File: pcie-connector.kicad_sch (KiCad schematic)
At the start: 7 parts, among them J2 PCIe_x16_10146070-113Y0LF-ver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

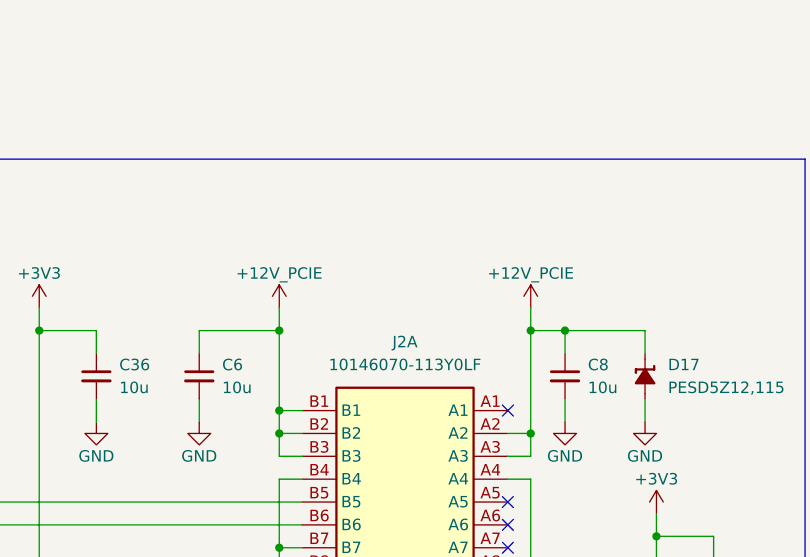
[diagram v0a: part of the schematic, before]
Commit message: [#79426] Removed power sequencing, added PERST control
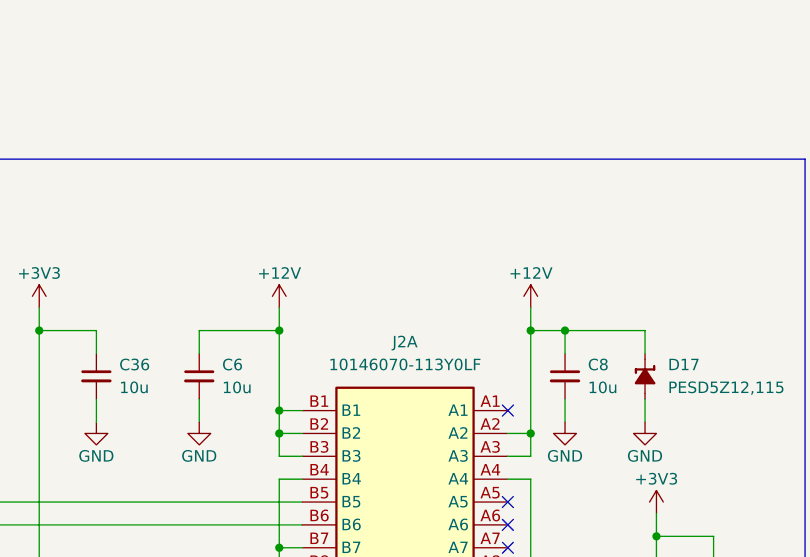
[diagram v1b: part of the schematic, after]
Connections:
- net +12V_PCIE renamed +12V
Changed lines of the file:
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@@
-	)
-	(symbol
-		(lib_id "antmicropower:+12V")
-		(at 147.32 91.44 0)
-		(unit 1)
-		(exclude_from_sim no)
-		(in_bom yes)
-		(on_board yes)
-		(dnp no)
-		(property "Reference" "#PWR06"
-			(at 147.32 95.25 0)
-			(effects
-				(font
-					(size 1.27 1.27)
-				)
-				(hide yes)
-			)
-		)
-		(property "Value" "+12V_PCIE"
-			(at 147.32 87.63 0)
-			(effects
-				(font
-					(size 1.27 1.27)
-				)
-			)
-		)
-		(property "Footprint" ""
-			(at 147.32 91.44 0)
-			(effects
-				(font
-					(size 1.27 1.27)
-				)
-				(hide yes)
-			)
-		)
-		(property "Datasheet" ""
-			(at 147.32 91.44 0)
-			(effects
-				(font
-					(size 1.27 1.27)
-				)
-				(hide yes)
-			)
-		)
-		(property "Description" ""
-			(at 147.32 91.44 0)
-			(effects
-				(font
-					(size 1.27 1.27)
-				)
-				(hide yes)
-			)
-		)
-		(pin "1"
-		)
-		(instances
-			(project "oculink-to-pcie-adapter"
-				(path "/44c3be85-0a18-4d93-a9a5-650ee09b6032/1dd577d8-5fbf-46d4-a369-3d141c3fbf7d"
-					(reference "#PWR06")
-					(unit 1)
-				)
-			)
-		)
 	)
 	(symbol
@@
 	)
 	(symbol
+		(lib_id "antmicropower:+12V_AON")
+		(at 147.32 91.44 0)
+		(unit 1)
+		(exclude_from_sim no)
+		(in_bom yes)
+		(on_board yes)
+		(dnp no)
+		(property "Reference" "#PWR06"
+			(at 147.32 95.25 0)
+			(effects
+				(font
+					(size 1.27 1.27)
+				)
+				(hide yes)
+			)
+		)
+		(property "Value" "+12V"
+			(at 147.32 87.63 0)
+			(effects
+				(font
+					(size 1.27 1.27)
+				)
+			)
+		)
+		(property "Footprint" ""
+			(at 147.32 91.44 0)
+			(effects
+				(font
+					(size 1.27 1.27)
+				)
+				(hide yes)
+			)
+		)
+		(property "Datasheet" ""
+			(at 147.32 91.44 0)
+			(effects
+				(font
+					(size 1.27 1.27)
+				)
+				(hide yes)
+			)
+		)
+		(property "Description" ""
+			(at 147.32 91.44 0)
+			(effects
+				(font
+					(size 1.27 1.27)
+				)
+				(hide yes)
+			)
+		)
+		(pin "1"
+		)
+		(instances
+			(project "oculink-to-pcie-adapter"
+				(path "/44c3be85-0a18-4d93-a9a5-650ee09b6032/1dd577d8-5fbf-46d4-a369-3d141c3fbf7d"
+					(reference "#PWR06")
+					(unit 1)
+				)
+			)
+		)
+	)
+	(symbol
 		(lib_id "antmicropower:GND")
 		(at 292.1 208.28 0)
@@
 	)
 	(symbol
+		(lib_id "antmicropower:+12V_AON")
+		(at 175.26 91.44 0)
+		(unit 1)
+		(exclude_from_sim no)
+		(in_bom yes)
+		(on_board yes)
+		(dnp no)
+		(property "Reference" "#PWR03"
+			(at 175.26 95.25 0)
+			(effects
+				(font
+					(size 1.27 1.27)
+				)
+				(hide yes)
+			)
+		)
+		(property "Value" "+12V"
+			(at 175.26 87.63 0)
+			(effects
+				(font
+					(size 1.27 1.27)
+				)
+			)
+		)
+		(property "Footprint" ""
+			(at 175.26 91.44 0)
+			(effects
+				(font
+					(size 1.27 1.27)
+				)
+				(hide yes)
+			)
+		)
+		(property "Datasheet" ""
+			(at 175.26 91.44 0)
+			(effects
+				(font
+					(size 1.27 1.27)
+				)
+				(hide yes)
+			)
+		)
+		(property "Description" ""
+			(at 175.26 91.44 0)
+			(effects
+				(font
+					(size 1.27 1.27)
+				)
+				(hide yes)
+			)
+		)
+		(pin "1"
+		)
+		(instances
+			(project "oculink-to-pcie-adapter"
+				(path "/44c3be85-0a18-4d93-a9a5-650ee09b6032/1dd577d8-5fbf-46d4-a369-3d141c3fbf7d"
+					(reference "#PWR03")
+					(unit 1)
+				)
+			)
+		)
+	)
+	(symbol
 		(lib_id "antmicroTVSDiodes:PESD5Z12")
 		(at 187.96 96.52 270)
@@
 					(unit 1)
 				)
-			)
-		)
-	)
-	(symbol
-		(lib_id "antmicropower:+12V")
-		(at 175.26 91.44 0)
-		(unit 1)
-		(exclude_from_sim no)
-		(in_bom yes)
-		(on_board yes)
-		(dnp no)
-		(property "Reference" "#PWR03"
-			(at 175.26 95.25 0)
-			(effects
-				(font
-					(size 1.27 1.27)
-				)
-				(hide yes)
-			)
-		)
-		(property "Value" "+12V_PCIE"
-			(at 175.26 87.63 0)
-			(effects
-				(font
-					(size 1.27 1.27)
-				)
-			)
-		)
-		(property "Footprint" ""
-			(at 175.26 91.44 0)
-			(effects
-				(font
-					(size 1.27 1.27)
-				)
-				(hide yes)
-			)
-		)
-		(property "Datasheet" ""
-			(at 175.26 91.44 0)
-			(effects
-				(font
-					(size 1.27 1.27)
-				)
-				(hide yes)
-			)
-		)
-		(property "Description" ""
-			(at 175.26 91.44 0)
-			(effects
-				(font
-					(size 1.27 1.27)
-				)
-				(hide yes)
-			)
-		)
-		(pin "1"
-		)
-		(instances
-			(project ""
-				(path "/44c3be85-0a18-4d93-a9a5-650ee09b6032/1dd577d8-5fbf-46d4-a369-3d141c3fbf7d"
-					(reference "#PWR03")
-					(unit 1)
-				)

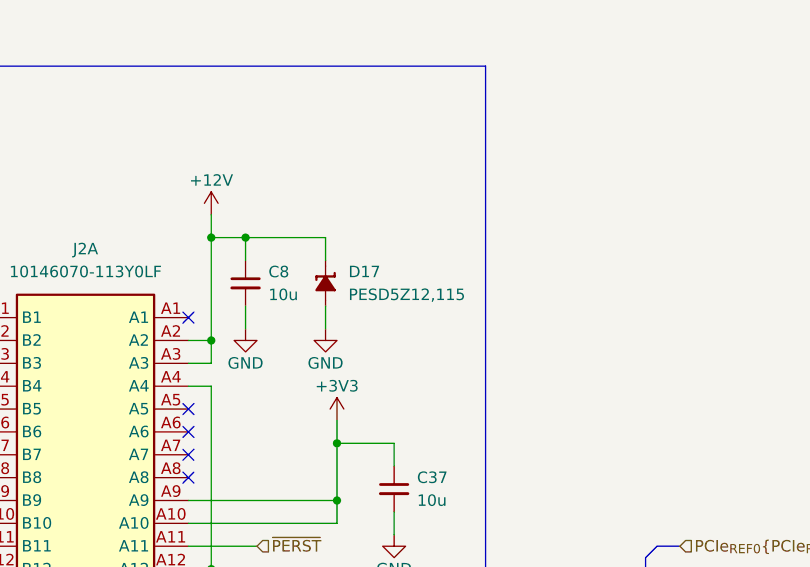
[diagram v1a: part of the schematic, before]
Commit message: [#79262] Route high speed and power
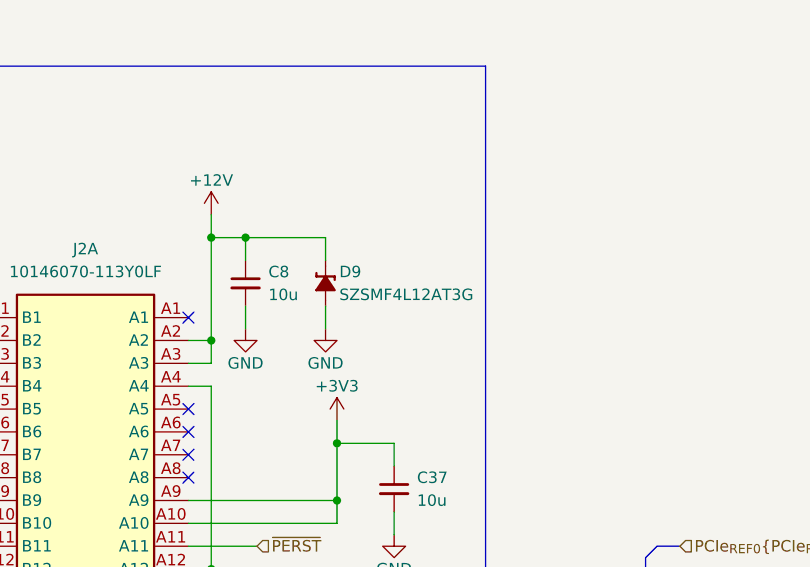
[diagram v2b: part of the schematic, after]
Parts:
- removed D17: PESD5Z12, antmicro-footprints:SOD-523, symbol antmicroTVSDiodes:PESD5Z12
- added D9: SZSMF4L14AT3G, antmicro-footprints:SOD-123FL, symbol antmicroTVSDiodes:SZSMF4L14AT3G
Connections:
- net +12V: now also D9.1 (C)
- net GND: now also D9.2 (A)
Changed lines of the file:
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@@
+	)
+	(symbol
+		(lib_id "antmicroTVSDiodes:SZSMF4L14AT3G")
+		(at 187.96 96.52 90)
+		(mirror x)
+		(unit 1)
+		(exclude_from_sim no)
+		(in_bom yes)
+		(on_board yes)
+		(dnp no)
+		(property "Reference" "D9"
+			(at 189.484 97.79 90)
+			(effects
+				(font
+					(size 1.27 1.27)
+					(thickness 0.15)
+				)
+				(justify right)
+			)
+		)
+		(property "Value" "SZSMF4L14AT3G"
+			(at 198.12 111.76 0)
+			(effects
+				(font
+					(size 1.27 1.27)
+					(thickness 0.15)
+				)
+				(justify left bottom)
+				(hide yes)
+			)
+		)
+		(property "Footprint" "antmicro-footprints:SOD-123FL"
+			(at 200.66 111.76 0)
+			(effects
+				(font
+					(size 1.27 1.27)
+					(thickness 0.15)
+				)
+				(justify left bottom)
+				(hide yes)
+			)
+		)
+		(property "Datasheet" "https://www.mouser.com/datasheet/2/240/media-3320461.pdf"
+			(at 203.2 111.76 0)
+			(effects
+				(font
+					(size 1.27 1.27)
+					(thickness 0.15)
+				)
+				(justify left bottom)
+				(hide yes)
+			)
+		)
+		(property "Description" "ESD, TVS Diode, 14V, UNI, 400W, SOD-123FL"
+			(at 187.96 96.52 0)
+			(effects
+				(font
+					(size 1.27 1.27)
+				)
+				(hide yes)
+			)
+		)
+		(property "MPN" "SZSMF4L12AT3G"
+			(at 189.484 100.33 90)
+			(effects
+				(font
+					(size 1.27 1.27)
+					(thickness 0.15)
+				)
+				(justify right)
+			)
+		)
+		(property "Author" "Antmicro"
+			(at 205.74 111.76 0)
+			(effects
+				(font
+					(size 1.27 1.27)
+					(thickness 0.15)
+				)
+				(justify left bottom)
+				(hide yes)
+			)
+		)
+		(property "License" "Apache-2.0"
+			(at 208.28 111.76 0)
+			(effects
+				(font
+					(size 1.27 1.27)
+					(thickness 0.15)
+				)
+				(justify left bottom)
+				(hide yes)
+			)
+		)
+		(property "Manufacturer" "Littelfuse"
+			(at 210.82 111.76 0)
+			(effects
+				(font
+					(size 1.27 1.27)
+					(thickness 0.15)
+				)
+				(justify left bottom)
+				(hide yes)
+			)
+		)
+		(pin "1"
+		)
+		(pin "2"
+		)
+		(instances
+			(project "oculink-to-pcie-adapter"
+				(path "/44c3be85-0a18-4d93-a9a5-650ee09b6032/1dd577d8-5fbf-46d4-a369-3d141c3fbf7d"
+					(reference "D9")
+					(unit 1)
+				)
+			)
+		)
 	)
 	(symbol
@@
 					(unit 1)
 				)
-			)
-		)
-	)
-	(symbol
-		(lib_id "antmicroTVSDiodes:PESD5Z12")
-		(at 187.96 96.52 270)
-		(unit 1)
-		(exclude_from_sim no)
-		(in_bom yes)
-		(on_board yes)
-		(dnp no)
-		(property "Reference" "D17"
-			(at 190.5 97.79 90)
-			(effects
-				(font
-					(size 1.27 1.27)
-					(thickness 0.15)
-				)
-				(justify left)
-			)
-		)
-		(property "Value" "PESD5Z12"
-			(at 175.26 111.76 0)
-			(effects
-				(font
-					(size 1.27 1.27)
-					(thickness 0.15)
-				)
-				(justify left bottom)
-				(hide yes)
-			)
-		)
-		(property "Footprint" "antmicro-footprints:SOD-523"
-			(at 182.88 111.76 0)
-			(effects
-				(font
-					(size 1.27 1.27)
-					(thickness 0.15)
-				)
-				(justify left bottom)
-				(hide yes)
-			)
-		)
-		(property "Datasheet" "https://assets.nexperia.com/documents/data-sheet/PESD5Z12.pdf"
-			(at 180.34 111.76 0)
-			(effects
-				(font
-					(size 1.27 1.27)
-					(thickness 0.15)
-				)
-				(justify left bottom)
-				(hide yes)
-			)
-		)
-		(property "Description" "Unidirectional TVS, 30 kV,  SOD-523, 12 V, 35 pF"
-			(at 187.96 96.52 0)
-			(effects
-				(font
-					(size 1.27 1.27)
-				)
-				(hide yes)
-			)
-		)
-		(property "Manufacturer" "Nexperia"
-			(at 177.8 111.76 0)
-			(effects
-				(font
-					(size 1.27 1.27)
-					(thickness 0.15)
-				)
-				(justify left bottom)
-				(hide yes)
-			)
-		)
-		(property "MPN" "PESD5Z12,115"
-			(at 190.5 100.33 90)
-			(effects
-				(font
-					(size 1.27 1.27)
-					(thickness 0.15)
-				)
-				(justify left)
-			)
-		)
-		(property "Author" "Antmicro"
-			(at 172.72 111.76 0)
-			(effects
-				(font
-					(size 1.27 1.27)
-					(thickness 0.15)
-				)
-				(justify left bottom)
-				(hide yes)
-			)
-		)
-		(property "License" "Apache-2.0"
-			(at 170.18 111.76 0)
-			(effects
-				(font
-					(size 1.27 1.27)
-					(thickness 0.15)
-				)
-				(justify left bottom)
-				(hide yes)
-			)
-		)
-		(pin "2"
-		)
-		(pin "1"
-		)
-		(instances
-			(project "oculink-to-pcie-adapter"
-				(path "/44c3be85-0a18-4d93-a9a5-650ee09b6032/1dd577d8-5fbf-46d4-a369-3d141c3fbf7d"
-					(reference "D17")
-					(unit 1)
-				)

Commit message: [#79262] DRC clean
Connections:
- net GND: now also J2.S1, J2.S2

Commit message: [#79790] Applied review fixes
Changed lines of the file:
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@@
 	)
 	(bus_entry
-		(at 222.25 135.89)
+		(at 231.14 135.89)
 		(size 1.27 -1.27)
 		(stroke
@@
 	)
 	(bus_entry
-		(at 222.25 133.35)
+		(at 231.14 133.35)
 		(size 1.27 -1.27)
 		(stroke
@@
 	(bus
 		(pts
-			(xy 223.52 132.08) (xy 223.52 129.54)
+			(xy 232.41 132.08) (xy 232.41 129.54)
 		)
 		(stroke
@@
 	(bus
 		(pts
-			(xy 224.79 128.27) (xy 227.33 128.27)
+			(xy 233.68 128.27) (xy 236.22 128.27)
 		)
 		(stroke
@@
 	(bus
 		(pts
-			(xy 223.52 129.54) (xy 224.79 128.27)
+			(xy 232.41 129.54) (xy 233.68 128.27)
 		)
 		(stroke
@@
 	(bus
 		(pts
-			(xy 223.52 134.62) (xy 223.52 132.08)
+			(xy 232.41 134.62) (xy 232.41 132.08)
 		)
 		(stroke
@@
 	(wire
 		(pts
+			(xy 172.72 133.35) (xy 231.14 133.35)
+		)
+		(stroke
+			(width 0)
+			(type default)
+		)
+	)
+	(wire
+		(pts
 			(xy 120.65 93.98) (xy 127 93.98)
 		)
@@
 	(wire
 		(pts
-			(xy 172.72 135.89) (xy 222.25 135.89)
-		)
-		(stroke
-			(width 0)
-			(type default)
-		)
-	)
-	(wire
-		(pts
 			(xy 264.16 130.81) (xy 266.7 130.81)
 		)
@@
 	(wire
 		(pts
-			(xy 172.72 133.35) (xy 222.25 133.35)
+			(xy 172.72 135.89) (xy 231.14 135.89)
 		)
 		(stroke
@@
 	)
 	(label "PCIe_{REF0}.CK+"
-		(at 220.98 133.35 180)
+		(at 229.87 133.35 180)
 		(effects
 			(font
@@
 	)
 	(label "PCIe_{REF0}.CK-"
-		(at 220.98 135.89 180)
+		(at 229.87 135.89 180)
 		(effects
 			(font
@@
 	(hierarchical_label "PCIe_{REF0}{PCIe_{REF}}"
 		(shape input)
-		(at 227.33 128.27 0)
+		(at 236.22 128.27 0)
 		(effects
 			(font
